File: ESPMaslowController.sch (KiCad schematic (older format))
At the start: 40 parts, among them J1 Barrel_Jack_Switch, J10 Conn_01x03, J11 Conn_01x03, J2 B6B-PH-K-S, J3 B6B-PH-K-S, J4 B6B-PH-K-S, J5 B6B-PH-K-S, J6 B6B-PH-K-S, J7 Micro_SD_Card_Det, J8 Conn_01x03, J9 Conn_02x12_Odd_Even, U1 NCP3063, U2 ESP32-DevKit-Doit, U3 ATmega328PB-AU

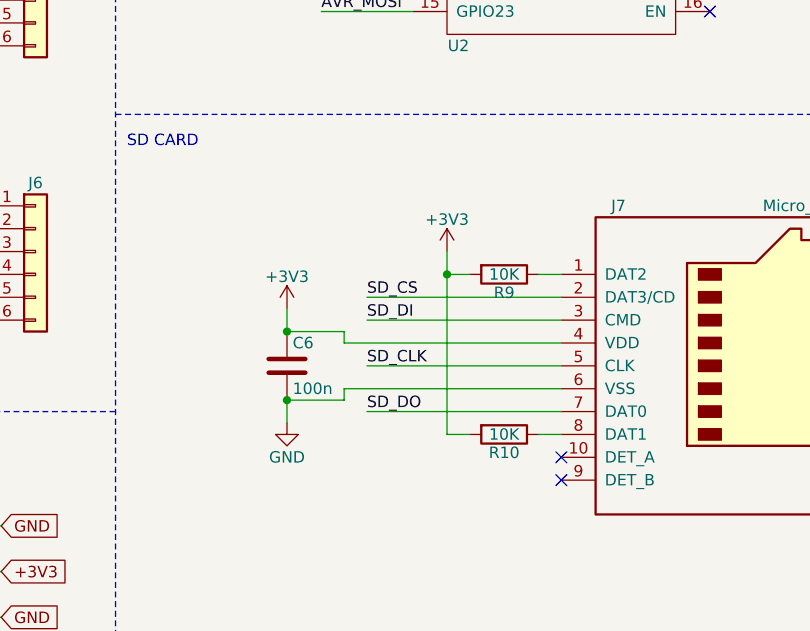
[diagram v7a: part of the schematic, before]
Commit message: Added pullup to SD CS line.
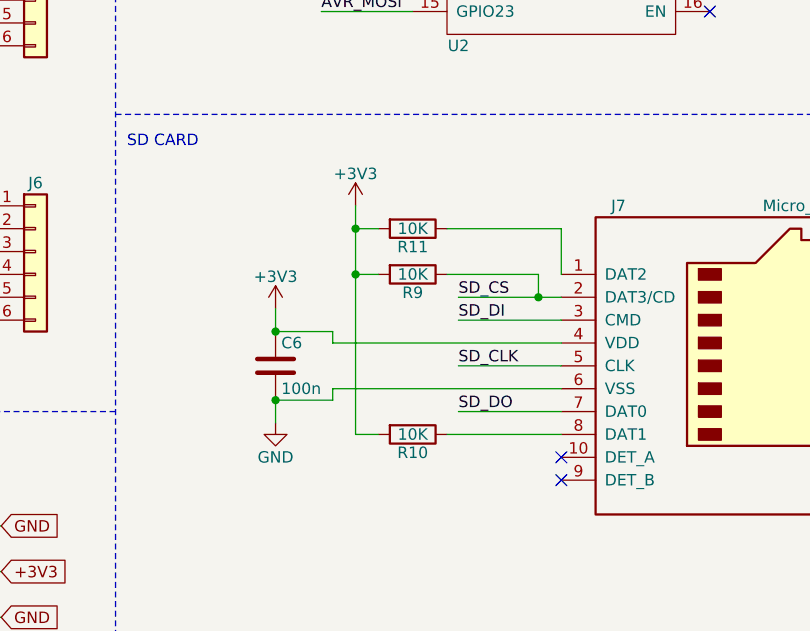
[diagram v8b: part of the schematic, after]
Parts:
- added R11: 10K, Resistor_SMD:R_0805_2012Metric, symbol Device:R
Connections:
- net +3V3: now also R11.2
- net SD_CS: now also R9.1
- net at J7.1 (DAT2): now also R11.1; no longer R9.1
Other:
- moved on the sheet: C6, R10, R9
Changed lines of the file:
@@
 Wire Wire Line
 	6950 3500 6950 3600
-Text Label 4900 6150 0    50   ~ 0
+Text Label 5300 6150 0    50   ~ 0
 SD_DI
-Text Label 4900 6550 0    50   ~ 0
+Text Label 5300 6550 0    50   ~ 0
 SD_DO
-Text Label 4900 6350 0    50   ~ 0
+Text Label 5300 6350 0    50   ~ 0
 SD_CLK
-Text Label 4900 6050 0    50   ~ 0
+Text Label 5300 6050 0    50   ~ 0
 SD_CS
 Wire Wire Line
-	5750 6050 4900 6050
-Wire Wire Line
-	5750 6150 4900 6150
-Wire Wire Line
-	5750 6350 4900 6350
-Wire Wire Line
-	5750 6550 4900 6550
+	5750 6050 5650 6050
+Wire Wire Line
+	5750 6150 5300 6150
+Wire Wire Line
+	5750 6350 5300 6350
+Wire Wire Line
+	5750 6550 5300 6550
 $Comp
 L power:+3V3 #PWR011
 U 1 1 5F6D002E
-P 4550 6100
-F 0 "#PWR011" H 4550 5950 50  0001 C CNN
-F 1 "+3V3" H 4550 6240 50  0000 C CNN
-F 2 "" H 4550 6100 50  0001 C CNN
-F 3 "" H 4550 6100 50  0001 C CNN
-	1    4550 6100
-	1    0    0    -1
-$EndComp
-Wire Wire Line
-	4550 6100 4550 6200
+P 4500 6100
+F 0 "#PWR011" H 4500 5950 50  0001 C CNN
+F 1 "+3V3" H 4500 6240 50  0000 C CNN
+F 2 "" H 4500 6100 50  0001 C CNN
+F 3 "" H 4500 6100 50  0001 C CNN
+	1    4500 6100
+	1    0    0    -1
+$EndComp
+Wire Wire Line
+	4500 6100 4500 6200
 $Comp
 L power:GND #PWR012
 U 1 1 5F6D1A5F
-P 4550 6600
-F 0 "#PWR012" H 4550 6350 50  0001 C CNN
-F 1 "GND" H 4550 6450 50  0000 C CNN
-F 2 "" H 4550 6600 50  0001 C CNN
-F 3 "" H 4550 6600 50  0001 C CNN
-	1    4550 6600
-	1    0    0    -1
-$EndComp
-Wire Wire Line
-	5750 6450 4800 6450
+P 4500 6600
+F 0 "#PWR012" H 4500 6350 50  0001 C CNN
+F 1 "GND" H 4500 6450 50  0000 C CNN
+F 2 "" H 4500 6600 50  0001 C CNN
+F 3 "" H 4500 6600 50  0001 C CNN
+	1    4500 6600
+	1    0    0    -1
+$EndComp
+Wire Wire Line
+	5750 6450 4750 6450
 $Comp
 L Device:C C6
 U 1 1 5F6D43E4
-P 4550 6350
-F 0 "C6" H 4575 6450 50  0000 L CNN
-F 1 "100n" H 4575 6250 50  0000 L CNN
-F 2 "Capacitor_SMD:C_0805_2012Metric" H 4588 6200 50  0001 C CNN
-F 3 "https://www.yageo.com/upload/media/product/productsearch/datasheet/mlcc/UPY-GPHC_X7R_6.3V-to-50V_18.pdf" H 4550 6350 50  0001 C CNN
-F 4 "Yageo" H 4550 6350 50  0001 C CNN "MFR"
-F 5 "CC0805KRX7R9BB104" H 4550 6350 50  0001 C CNN "MPN"
-F 6 "0.046" H 4550 6350 50  0001 C CNN "Price"
-F 7 "" H 4550 6350 50  0001 C CNN "SKU"
-F 8 "C49678" H 4550 6350 50  0001 C CNN "LCSC"
-	1    4550 6350
-	1    0    0    -1
-$EndComp
-Wire Wire Line
-	4800 6250 4800 6200
-Wire Wire Line
-	4550 6200 4800 6200
-Wire Wire Line
-	4800 6250 5750 6250
-Connection ~ 4550 6200
-Wire Wire Line
-	4800 6450 4800 6500
-Wire Wire Line
-	4800 6500 4550 6500
-Wire Wire Line
-	4550 6500 4550 6600
-Connection ~ 4550 6500
+P 4500 6350
+F 0 "C6" H 4525 6450 50  0000 L CNN
+F 1 "100n" H 4525 6250 50  0000 L CNN
+F 2 "Capacitor_SMD:C_0805_2012Metric" H 4538 6200 50  0001 C CNN
+F 3 "https://www.yageo.com/upload/media/product/productsearch/datasheet/mlcc/UPY-GPHC_X7R_6.3V-to-50V_18.pdf" H 4500 6350 50  0001 C CNN
+F 4 "Yageo" H 4500 6350 50  0001 C CNN "MFR"
+F 5 "CC0805KRX7R9BB104" H 4500 6350 50  0001 C CNN "MPN"
+F 6 "0.046" H 4500 6350 50  0001 C CNN "Price"
+F 7 "" H 4500 6350 50  0001 C CNN "SKU"
+F 8 "C49678" H 4500 6350 50  0001 C CNN "LCSC"
+	1    4500 6350
+	1    0    0    -1
+$EndComp
+Wire Wire Line
+	4750 6250 4750 6200
+Wire Wire Line
+	4500 6200 4750 6200
+Wire Wire Line
+	4750 6250 5750 6250
+Connection ~ 4500 6200
+Wire Wire Line
+	4750 6450 4750 6500
+Wire Wire Line
+	4750 6500 4500 6500
+Wire Wire Line
+	4500 6500 4500 6600
+Connection ~ 4500 6500
 NoConn ~ 5750 6750
 NoConn ~ 5750 6850
@@
 L power:+3V3 #PWR0101
 U 1 1 5F868927
-P 5250 5850
-F 0 "#PWR0101" H 5250 5700 50  0001 C CNN
-F 1 "+3V3" H 5250 5990 50  0000 C CNN
-F 2 "" H 5250 5850 50  0001 C CNN
-F 3 "" H 5250 5850 50  0001 C CNN
-	1    5250 5850
+P 4850 5650
+F 0 "#PWR0101" H 4850 5500 50  0001 C CNN
+F 1 "+3V3" H 4850 5790 50  0000 C CNN
+F 2 "" H 4850 5650 50  0001 C CNN
+F 3 "" H 4850 5650 50  0001 C CNN
+	1    4850 5650
 	1    0    0    -1
 $EndComp
@@
 L Device:R R?
 U 1 1 5F8850B1
-P 5500 5950
+P 5100 5950
 AR Path="/5F746CB5/5F8850B1" Ref="R?"  Part="1"
 AR Path="/5F8850B1" Ref="R9"  Part="1"
-F 0 "R9" V 5580 5950 50  0000 C CNN
-F 1 "10K" V 5500 5950 50  0000 C CNN
-F 2 "Resistor_SMD:R_0805_2012Metric" V 5430 5950 50  0001 C CNN
-F 3 "https://www.yageo.com/upload/media/product/productsearch/datasheet/rchip/PYu-RC_Group_51_RoHS_L_11.pdf" H 5500 5950 50  0001 C CNN
-F 4 "Yageo" H 5500 5950 50  0001 C CNN "MFR"
-F 5 "RC0805FR-0710KL" H 5500 5950 50  0001 C CNN "MPN"
-F 6 "0.10" H 5500 5950 50  0001 C CNN "Price"
-F 7 "C17414" H 5500 5950 50  0001 C CNN "LCSC"
-	1    5500 5950
+F 0 "R9" V 5180 5950 50  0000 C CNN
+F 1 "10K" V 5100 5950 50  0000 C CNN
+F 2 "Resistor_SMD:R_0805_2012Metric" V 5030 5950 50  0001 C CNN
+F 3 "https://www.yageo.com/upload/media/product/productsearch/datasheet/rchip/PYu-RC_Group_51_RoHS_L_11.pdf" H 5100 5950 50  0001 C CNN
+F 4 "Yageo" H 5100 5950 50  0001 C CNN "MFR"
+F 5 "RC0805FR-0710KL" H 5100 5950 50  0001 C CNN "MPN"
+F 6 "0.10" H 5100 5950 50  0001 C CNN "Price"
+F 7 "C17414" H 5100 5950 50  0001 C CNN "LCSC"
+	1    5100 5950
 	0    1    1    0
 $EndComp
@@
 L Device:R R?
 U 1 1 5F885CFB
-P 5500 6650
+P 5100 6650
 AR Path="/5F746CB5/5F885CFB" Ref="R?"  Part="1"
 AR Path="/5F885CFB" Ref="R10"  Part="1"
-F 0 "R10" V 5580 6650 50  0000 C CNN
-F 1 "10K" V 5500 6650 50  0000 C CNN
-F 2 "Resistor_SMD:R_0805_2012Metric" V 5430 6650 50  0001 C CNN
-F 3 "https://www.yageo.com/upload/media/product/productsearch/datasheet/rchip/PYu-RC_Group_51_RoHS_L_11.pdf" H 5500 6650 50  0001 C CNN
-F 4 "Yageo" H 5500 6650 50  0001 C CNN "MFR"
-F 5 "RC0805FR-0710KL" H 5500 6650 50  0001 C CNN "MPN"
-F 6 "0.10" H 5500 6650 50  0001 C CNN "Price"
-F 7 "C17414" H 5500 6650 50  0001 C CNN "LCSC"
-	1    5500 6650
+F 0 "R10" V 5180 6650 50  0000 C CNN
+F 1 "10K" V 5100 6650 50  0000 C CNN
+F 2 "Resistor_SMD:R_0805_2012Metric" V 5030 6650 50  0001 C CNN
+F 3 "https://www.yageo.com/upload/media/product/productsearch/datasheet/rchip/PYu-RC_Group_51_RoHS_L_11.pdf" H 5100 6650 50  0001 C CNN
+F 4 "Yageo" H 5100 6650 50  0001 C CNN "MFR"
+F 5 "RC0805FR-0710KL" H 5100 6650 50  0001 C CNN "MPN"
+F 6 "0.10" H 5100 6650 50  0001 C CNN "Price"
+F 7 "C17414" H 5100 6650 50  0001 C CNN "LCSC"
+	1    5100 6650
 	0    1    1    0
 $EndComp
 Wire Wire Line
-	5650 6650 5750 6650
-Wire Wire Line
-	5650 5950 5750 5950
-Wire Wire Line
-	5350 6650 5250 6650
-Wire Wire Line
-	5250 6650 5250 5950
-Wire Wire Line
-	5250 5950 5350 5950
-Wire Wire Line
-	5250 5850 5250 5950
-Connection ~ 5250 5950
+	5250 6650 5750 6650
+Wire Wire Line
+	4950 6650 4850 6650
+Wire Wire Line
+	4850 6650 4850 5950
+Wire Wire Line
+	4850 5950 4950 5950
+Wire Wire Line
+	4850 5650 4850 5750
+Connection ~ 4850 5950
+$Comp
+L Device:R R?
+U 1 1 5F86A2EC
+P 5100 5750
+AR Path="/5F746CB5/5F86A2EC" Ref="R?"  Part="1"
+AR Path="/5F86A2EC" Ref="R11"  Part="1"
+F 0 "R11" V 5180 5750 50  0000 C CNN
+F 1 "10K" V 5100 5750 50  0000 C CNN
+F 2 "Resistor_SMD:R_0805_2012Metric" V 5030 5750 50  0001 C CNN
+F 3 "https://www.yageo.com/upload/media/product/productsearch/datasheet/rchip/PYu-RC_Group_51_RoHS_L_11.pdf" H 5100 5750 50  0001 C CNN
+F 4 "Yageo" H 5100 5750 50  0001 C CNN "MFR"
+F 5 "RC0805FR-0710KL" H 5100 5750 50  0001 C CNN "MPN"
+F 6 "0.10" H 5100 5750 50  0001 C CNN "Price"
+F 7 "C17414" H 5100 5750 50  0001 C CNN "LCSC"
+	1    5100 5750
+	0    1    1    0
+$EndComp
+Wire Wire Line
+	4850 5750 4950 5750
+Connection ~ 4850 5750
+Wire Wire Line
+	4850 5750 4850 5950
+Wire Wire Line
+	5250 5950 5650 5950
+Wire Wire Line
+	5650 5950 5650 6050
+Connection ~ 5650 6050
+Wire Wire Line
+	5650 6050 5300 6050
+Wire Wire Line
+	5750 5950 5750 5750
+Wire Wire Line
+	5750 5750 5250 5750
 $EndSCHEMATC
